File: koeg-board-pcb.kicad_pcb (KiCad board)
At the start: 4 copper layers, 228.3 x 84.3 mm, 233 parts, among them J1 Conn_01x02, J2 SWD_Connector, J3 USB_C_Receptacle_USB2.0_16P, J4 Conn_01x02, J5 SWD_Connector, J6 USB_C_Receptacle_USB2.0_16P, Q1 BSS138, Q2 BSS138, SW1 Reset Button, SW10 SW_Push, SW11 SW_Push, SW12 SW_Push, SW13 SW_Push, SW14 SW_Push, SW15 SW_Push, SW16 SW_Push, SW17 SW_Push, SW18 SW_Push, SW19 SW_Push, SW2 SW_On_Off, SW20 SW_Push, SW21 SW_Push, SW22 SW_Push, SW23 SW_Push, SW24 Reset Button, SW25 SW_On_Off, SW26 SW_Push, SW27 SW_Push, SW28 SW_Push, SW29 SW_Push, SW3 SW_Push, SW30 SW_Push, SW31 SW_Push, SW32 SW_Push, SW33 SW_Push, SW34 SW_Push, SW35 SW_Push, SW36 SW_Push, SW37 SW_Push, SW38 SW_Push, SW39 SW_Push, SW4 SW_Push, SW40 SW_Push, SW41 SW_Push, SW42 SW_Push, SW43 SW_Push, SW44 SW_Push, SW45 SW_Push, SW46 SW_Push, SW5 SW_Push, SW6 SW_Push, SW7 SW_Push, SW8 SW_Push, SW9 SW_Push, U2 USBLC6-2SC6, U4 TPS61252DSG, U5 USBLC6-2SC6, U6 TPS61252DSG, U7 nRF52833_QDxx, U8 nRF52833_QDxx, Y1 32MHz, Y2 32MHz, Y3 32.768 kHz, Y4 32.768 kHz

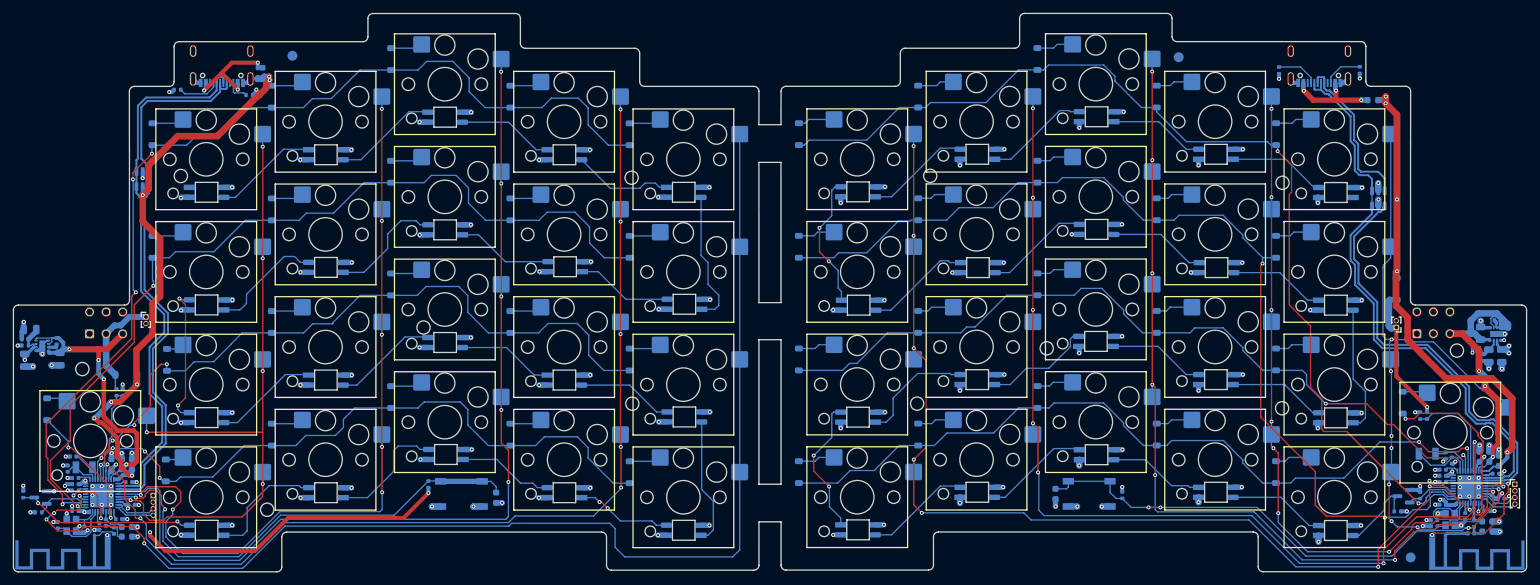
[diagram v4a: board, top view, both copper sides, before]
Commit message: finished power circuit
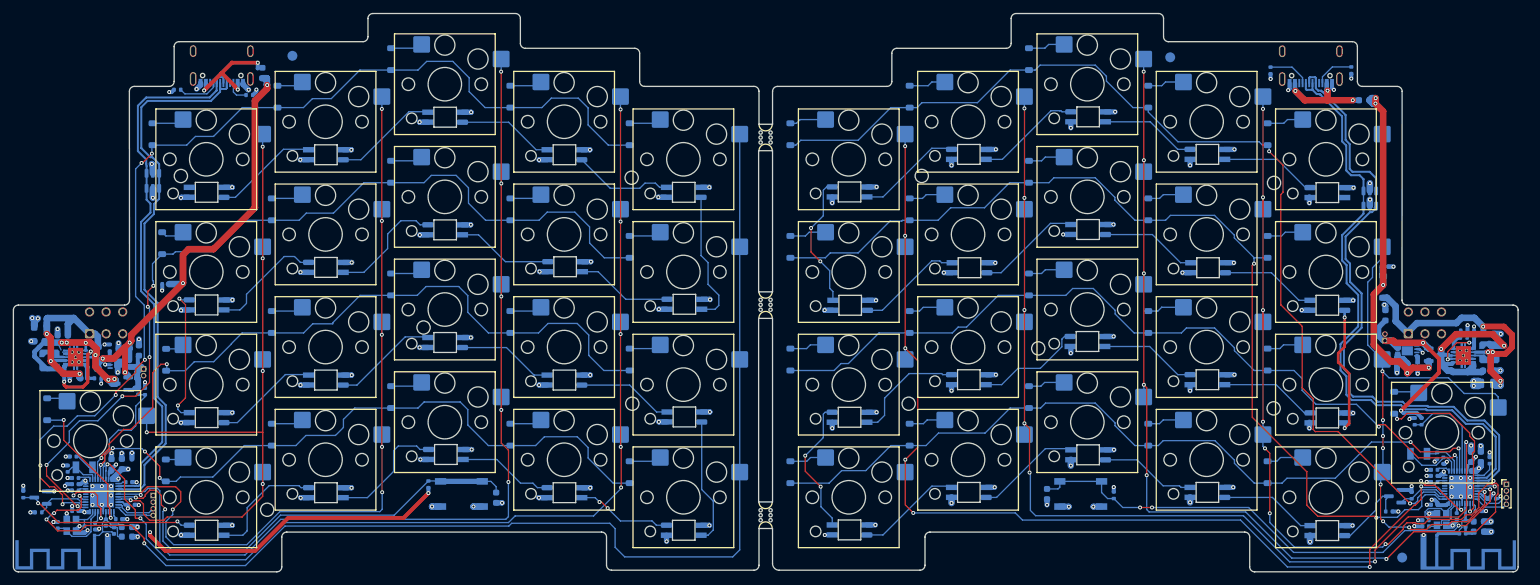
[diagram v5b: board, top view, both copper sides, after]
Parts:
- removed H11, H12: MountingHole, MountingHole:MountingHole_2mm
- removed L3, L8: 1uH, Inductor_SMD:L_0402_1005Metric
- removed R16: 786k, Resistor_SMD:R_0402_1005Metric
- removed R18: 243k, Resistor_SMD:R_0402_1005Metric
- added C24: 4.7uF, Capacitor_SMD:C_0603_1608Metric, B.Cu at (47.6, 122.2)
- added C45: 100uf, Capacitor_SMD:C_0805_2012Metric, B.Cu at (253.6, 110.0)
- added C46: 100uf, Capacitor_SMD:C_0805_2012Metric, B.Cu at (35.3, 101.4)
- added C8: 10uF, Capacitor_SMD:C_0603_1608Metric, B.Cu at (253.8, 108.1)
- added L1: 2.2uH, LPS3015-222MRC:IND_LPS3015-222MRC, B.Cu at (253.9, 105.3)
- added L2: 2.2uH, LPS3015-222MRC:IND_LPS3015-222MRC, B.Cu at (36.7, 106.6)
- added Q3: AO3401A, Package_TO_SOT_SMD:SOT-23, B.Cu at (245.7, 105.7)
- added Q4: AO3401A, Package_TO_SOT_SMD:SOT-23, B.Cu at (47.6, 110.1)
- added R19: 10k, Resistor_SMD:R_0402_1005Metric, B.Cu at (54.2, 95.0)
- added R21: 2k, Resistor_SMD:R_0402_1005Metric, B.Cu at (45.8, 104.7)
- added R23: 1.8M, Resistor_SMD:R_0402_1005Metric, B.Cu at (250.1, 103.1)
- added R24: 1.8M, Resistor_SMD:R_0402_1005Metric, B.Cu at (41.9, 109.3)
- added R25: 200k, Resistor_SMD:R_0402_1005Metric, B.Cu at (250.1, 102.0)
- added R26: 200k, Resistor_SMD:R_0402_1005Metric, B.Cu at (44.0, 109.3)
- added U1: MCP73831-2-MC, Package_DFN_QFN:DFN-8-1EP_3x2mm_P0.5mm_EP1.7x1.4mm, B.Cu at (241.6, 105.1)
- added U3: TPS61200DRC, Package_SON:Texas_S-PVSON-N10_ThermalVias, B.Cu at (250.0, 105.8)
- added mouse-bite-2mm-slot: VAL**, panelization:mouse-bite-2mm-slot, F.Cu at (144.7, 72.9)
- added mouse-bite-2mm-slot: VAL**, panelization:mouse-bite-2mm-slot, F.Cu at (144.7, 98.2)
- added mouse-bite-2mm-slot: VAL**, panelization:mouse-bite-2mm-slot, F.Cu at (144.7, 129.9)
- AE1: footprint pcb_ant:pcb_antenna -> pcb_ant:flipped_pcb_antenna
- AE2: footprint pcb_ant:flipped_pcb_antenna -> pcb_ant:pcb_antenna
- C1: value 4.7uF -> 47uF
- C17: value 4.7uF -> 1uF; footprint Capacitor_SMD:C_0603_1608Metric -> Capacitor_SMD:C_0402_1005Metric
- C33: value 100pF -> 22uF; footprint Capacitor_SMD:C_0805_2012Metric -> Capacitor_SMD:C_0603_1608Metric
- C34: value 100pF -> 47uF; footprint Capacitor_SMD:C_0805_2012Metric -> Capacitor_SMD:C_0603_1608Metric
- C35: value 22uF -> 4.7uF; footprint Capacitor_SMD:C_0805_2012Metric -> Capacitor_SMD:C_0603_1608Metric
- C36: value 22uF -> 10uF; footprint Capacitor_SMD:C_0805_2012Metric -> Capacitor_SMD:C_0603_1608Metric
- C37: footprint Capacitor_SMD:C_0805_2012Metric -> Capacitor_SMD:C_0402_1005Metric
- C38: value 1uF -> 22uF; footprint Capacitor_SMD:C_0805_2012Metric -> Capacitor_SMD:C_0603_1608Metric
- D1, D43: value 1N5819 -> D_Schottky
- J1, J4: moved to B.Cu
- R15: value 786k -> 10k
- R17: value 243k -> 2k
- U4: value TPS61252DSG -> MCP73831-2-MC; footprint Package_SON:WSON-8-1EP_2x2mm_P0.5mm_EP0.9x1.6mm -> Package_DFN_QFN:DFN-8-1EP_3x2mm_P0.5mm_EP1.7x1.4mm
- U6: value TPS61252DSG -> TPS61200DRC; footprint Package_SON:WSON-8-1EP_2x2mm_P0.5mm_EP0.9x1.6mm -> Package_SON:Texas_S-PVSON-N10_ThermalVias
- moved C37 213.3 mm to (39.4, 108.9), turned to 0 degrees
- moved U4 207.6 mm to (47.3, 107.0), turned to 180 degrees
- moved C35 205.7 mm to (50.2, 105.1), turned to 90 degrees
- moved C19 205.1 mm to (252.7, 121.1)
- moved C17 203.5 mm to (251.6, 102.6)
- moved AE1 202.5 mm to (44.2, 133.2)
- moved AE2 201.2 mm to (245.3, 133.2)
- moved C3 26.5 mm to (238.3, 99.7)
- moved C1 20.4 mm to (240.8, 107.5), turned to 0 degrees
- moved R15 19.7 mm to (238.2, 92.4), turned to 0 degrees
- moved C34 14.4 mm to (47.9, 104.9)
- moved R17 9.20 mm to (243.1, 107.4), turned to -90 degrees
- moved J4 7.88 mm to (50.9, 107.9), turned to 180 degrees
- moved U6 5.31 mm to (40.6, 106.1)
- moved D43 5.01 mm to (44.0, 106.2), turned to -90 degrees
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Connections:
- AE1 pad 2: Net-(AE1-PCB_Trace) -> /right/ANT
- AE2 pad 2: Net-(AE2-PCB_Trace) -> /left/ANT
- C1 pad 1: /left/5V -> GND
- C1 pad 2: GND -> /left/power/USB-5V
- C17 pad 1: /right/5V -> Net-(U3-UVLO)
- C19 pad 1: /right/3.2V-5V -> /left/5V
- C3 pad 1: /left/3.2V-5V -> /left/VBAT
- C33 pad 1: /left/leds/LED_5V -> /left/power/Boost-Output
- C33 pad 2: Net-(U4-FB) -> GND
- C34 pad 1: /right/leds/LED_5V -> GND
- C34 pad 2: Net-(U6-FB) -> /right/power/USB-5V
- C35 pad 1: /left/leds/LED_5V -> /right/VBAT
- C36 pad 1: /right/leds/LED_5V -> GND
- C36 pad 2: GND -> /right/power/Boost-Input
- C37 pad 1: /left/3.2V-5V -> Net-(U6-UVLO)
- C38 pad 1: /right/3.2V-5V -> /right/power/Boost-Output
- D1 pad 1: /left/VBAT -> /left/power/Boost-Output
- D1 pad 2: /left/5V -> /left/power/USB-5V
- D23 pad 4: /left/leds/LED_5V -> /left/5V
- D24 pad 4: /left/leds/LED_5V -> /left/5V
- D25 pad 4: /left/leds/LED_5V -> /left/5V
- D26 pad 4: /left/leds/LED_5V -> /left/5V
- D27 pad 4: /left/leds/LED_5V -> /left/5V
- D28 pad 4: /left/leds/LED_5V -> /left/5V
- D29 pad 4: /left/leds/LED_5V -> /left/5V
- D30 pad 4: /left/leds/LED_5V -> /left/5V
- D31 pad 4: /left/leds/LED_5V -> /left/5V
- D32 pad 4: /left/leds/LED_5V -> /left/5V
- D33 pad 4: /left/leds/LED_5V -> /left/5V
- D34 pad 4: /left/leds/LED_5V -> /left/5V
- D35 pad 4: /left/leds/LED_5V -> /left/5V
- D36 pad 4: /left/leds/LED_5V -> /left/5V
- D37 pad 4: /left/leds/LED_5V -> /left/5V
- D38 pad 4: /left/leds/LED_5V -> /left/5V
- D39 pad 4: /left/leds/LED_5V -> /left/5V
- D40 pad 4: /left/leds/LED_5V -> /left/5V
- D41 pad 4: /left/leds/LED_5V -> /left/5V
- D42 pad 4: /left/leds/LED_5V -> /left/5V
- D43 pad 1: /right/VBAT -> /right/power/Boost-Output
- D43 pad 2: /right/5V -> /right/power/USB-5V
- D65 pad 4: /right/leds/LED_5V -> /right/5V
- D66 pad 4: /right/leds/LED_5V -> /right/5V
- D67 pad 4: /right/leds/LED_5V -> /right/5V
- D68 pad 4: /right/leds/LED_5V -> /right/5V
- D69 pad 4: /right/leds/LED_5V -> /right/5V
- D70 pad 4: /right/leds/LED_5V -> /right/5V
- D71 pad 4: /right/leds/LED_5V -> /right/5V
- D72 pad 4: /right/leds/LED_5V -> /right/5V
- D73 pad 4: /right/leds/LED_5V -> /right/5V
- D74 pad 4: /right/leds/LED_5V -> /right/5V
- D75 pad 4: /right/leds/LED_5V -> /right/5V
- D76 pad 4: /right/leds/LED_5V -> /right/5V
- D77 pad 4: /right/leds/LED_5V -> /right/5V
- D78 pad 4: /right/leds/LED_5V -> /right/5V
- D79 pad 4: /right/leds/LED_5V -> /right/5V
- D80 pad 4: /right/leds/LED_5V -> /right/5V
- D81 pad 4: /right/leds/LED_5V -> /right/5V
- D82 pad 4: /right/leds/LED_5V -> /right/5V
- D83 pad 4: /right/leds/LED_5V -> /right/5V
- D84 pad 4: /right/leds/LED_5V -> /right/5V
- F1 pad 1: /left/5V -> /left/power/USB-5V
- F2 pad 1: /right/5V -> /right/power/USB-5V
- J3 pad S1: GND -> unconnected-(J3-SHIELD-PadS1)_3
- J6 pad S1: GND -> unconnected-(J6-SHIELD-PadS1)_2
- L10 pad 2: Net-(AE2-PCB_Trace) -> /right/ANT
- L5 pad 2: Net-(AE1-PCB_Trace) -> /left/ANT
- R14 pad 1: /right/leds/LED_5V -> /right/5V
- R15 pad 1: /left/leds/LED_5V -> /left/power/USB-5V
- R15 pad 2: Net-(U4-FB) -> GND
- R17 pad 1: Net-(U4-FB) -> Net-(U1-PROG)
- R7 pad 1: /left/leds/LED_5V -> /left/5V
- SW2 pad 1: unconnected-(SW2A-A-Pad1) -> /left/power/Boost-Output
- SW2 pad 2: /left/VBAT -> /left/5V
- SW2 pad 3: /left/3.2V-5V -> unconnected-(SW2A-C-Pad3)
- SW25 pad 1: unconnected-(SW25A-A-Pad1) -> /right/power/Boost-Output
- SW25 pad 2: /right/VBAT -> /right/5V
- SW25 pad 3: /right/3.2V-5V -> unconnected-(SW25A-C-Pad3)
- U4 pad 1: GND -> /right/power/USB-5V
- U4 pad 2: /left/leds/LED_5V -> /right/power/USB-5V
- U4 pad 3: Net-(U4-FB) -> /right/VBAT
- U4 pad 4: /left/3.2V-5V -> /right/VBAT
- U4 pad 5: GND -> unconnected-(U4-STAT-Pad5)
- U4 pad 6: /left/3.2V-5V -> GND
- U4 pad 7: Net-(U4-SW) -> unconnected-(U4-NC-Pad7)
- U4 pad 8: /left/3.2V-5V -> Net-(U4-PROG)
- U4 pad 9: GND -> (no net)
- U6 pad 1: GND -> Net-(U6-UVLO)
- U6 pad 2: /right/leds/LED_5V -> /right/power/Boost-Output
- U6 pad 3: Net-(U6-FB) -> Net-(U6-L)
- U6 pad 4: /right/3.2V-5V -> GND
- U6 pad 5: GND -> /right/power/Boost-Input
- U6 pad 6: /right/3.2V-5V -> /right/power/Boost-Input
- U6 pad 7: Net-(U6-SW) -> Net-(U6-UVLO)
- U6 pad 8: /right/3.2V-5V -> /right/power/Boost-Input
- U7 pad 9: /left/3.2V-5V -> /left/5V
- U8 pad 9: /right/3.2V-5V -> /right/5V
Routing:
- net /right/power/USB-5V: track 0.00 -> 68.0 mm, vias 0 -> 5
- net /right/5V: track 90.9 -> 31.1 mm, vias 7 -> 24
- net /left/power/USB-5V: track 0.00 -> 58.7 mm, vias 0 -> 5
- net /left/3.2V-5V: track 49.1 -> 0.00 mm, vias 3 -> 0
- net /right/3.2V-5V: track 46.2 -> 0.00 mm, vias 4 -> 0
- net /left/power/Boost-Output: track 0.00 -> 45.5 mm, vias 0 -> 5
- net /left/5V: track 78.6 -> 35.0 mm, vias 6 -> 23
- net /right/leds/LED_5V: track 31.7 -> 0.00 mm, vias 23 -> 0
- net /left/leds/LED_5V: track 29.1 -> 0.00 mm, vias 24 -> 0
- net /left/power/Boost-Input: track 0.00 -> 28.8 mm, vias 0 -> 2
- net /right/power/Boost-Output: track 0.00 -> 28.3 mm, vias 0 -> 3
- net /right/power/Boost-Input: track 0.00 -> 26.0 mm, vias 0 -> 6
- net Net-(U6-UVLO): track 0.00 -> 12.7 mm, vias 0 -> 2
- net GND: track 127.2 -> 138.5 mm, vias 118 -> 134
- net Net-(U3-UVLO): track 0.00 -> 8.09 mm, vias 0 -> 2
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- added copper zone on In1.Cu, net /left/5V
- added copper zone on In1.Cu, net /right/5V
- added copper zone on B.Cu, net /right/power/Boost-Input
- removed copper zone on In1.Cu, net /left/leds/LED_5V
- removed copper zone on In1.Cu, net /right/leds/LED_5V
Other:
- board size 228.3 x 84.3 mm -> 227.1 x 84.3 mm
